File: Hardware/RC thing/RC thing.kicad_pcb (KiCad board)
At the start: 2 copper layers, 56.4 x 52.8 mm, 68 parts, among them J2 2171790001, J2 Conn_01x04, SW1 Bat_switch, SW1 TL3342F160QG_TR, SW2 SW_Push, SW3 SW_Push, SW4 SW_Push, SW5 TL3342F160QG_TR, U1 MCP73831-2-OT, U102 NRF24L01_Breakout, U2 RP2040, U3 W25Q128JVS, U401 TPS62170DSG, Y3 Crystal_GND24_Small

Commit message: RC thing PCB 95% trustworthy (six seven)
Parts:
- removed C30: 100n, Capacitor_SMD:C_0603_1608Metric_Pad1.08x0.95mm_HandSolder
- removed the J2 at (160.2, 68.7)
- removed R25: 100k, Resistor_SMD:R_0603_1608Metric_Pad0.98x0.95mm_HandSolder
- removed R26: 360k, Resistor_SMD:R_0603_1608Metric_Pad0.98x0.95mm_HandSolder
- removed RV3, RV4: 4.7k, Connector_PinHeader_2.54mm:PinHeader_1x03_P2.54mm_Vertical
- removed U102: NRF24L01_Breakout, Connector_PinHeader_2.54mm:PinHeader_2x04_P2.54mm_Vertical
- added C409: 100n, Capacitor_SMD:C_0603_1608Metric_Pad1.08x0.95mm_HandSolder, B.Cu at (126.5, 67.4)
- added J1: Conn_01x04, Connector_PinHeader_2.54mm:PinHeader_1x04_P2.54mm_Vertical, B.Cu at (160.0, 68.5)
- added R410: 100k, Resistor_SMD:R_0603_1608Metric_Pad0.98x0.95mm_HandSolder, B.Cu at (124.5, 67.4)
- added R411: 360k, Resistor_SMD:R_0603_1608Metric_Pad0.98x0.95mm_HandSolder, B.Cu at (128.5, 67.4)
- added RV1: 4.7k, Connector_PinHeader_2.54mm:PinHeader_1x03_P2.54mm_Vertical, B.Cu at (127.5, 75.0)
- added RV2: 4.7k, Connector_PinHeader_2.54mm:PinHeader_1x03_P2.54mm_Vertical, B.Cu at (127.5, 71.0)
- added U101: NRF24L01_Breakout, Connector_PinHeader_2.54mm:PinHeader_2x04_P2.54mm_Vertical, B.Cu at (125.0, 81.0)
- moved SW4 1.85 mm to (156.5, 85.2)
- moved SW2 1.83 mm to (156.5, 76.0)
- moved SW3 1.77 mm to (156.5, 80.5)
- moved R2 0.53 mm to (129.0, 54.5)
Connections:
- D2 pad 1: /BMS and power/Charge_status -> /RP2040/GPIO22
- SW2 pad 2: /RP2040/Button1 -> /Button1
- SW3 pad 2: /RP2040/Button2 -> /Button2
- SW4 pad 2: /RP2040/Button3 -> /Button3
- U1 pad 1: /BMS and power/Charge_status -> /RP2040/GPIO22
- U2 pad 2: /RP2040/GPIO0 -> /SDA
- U2 pad 27: /RP2040/GPIO16 -> /MISO
- U2 pad 29: /RP2040/GPIO18 -> /SCK
- U2 pad 3: /RP2040/GPIO1 -> /SCL
- U2 pad 30: /RP2040/GPIO19 -> /MOSI
- U2 pad 31: /RP2040/GPIO20 -> /CE
- U2 pad 32: /RP2040/GPIO21 -> /CSN
- U2 pad 38: /RP2040/GPIO26_ADC0 -> /AnaStk_1
- U2 pad 39: /RP2040/GPIO27_ADC1 -> /AnaStk_2
- U2 pad 6: /RP2040/GPIO4 -> /Button1
- U2 pad 7: /RP2040/GPIO5 -> /Button2
- U2 pad 8: /RP2040/GPIO6 -> /Button3
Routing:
- net /RP2040/GPIO22: track 0.00 -> 30.2 mm, vias 0 -> 2
- net (no net): track 30.2 -> 0.00 mm
- net /Button3: track 0.00 -> 17.1 mm
- net /RP2040/CSN: track 16.4 -> 0.00 mm
- net /CSN: track 0.00 -> 16.4 mm
- net /RP2040/Battery_voltage_level: track 15.3 -> 0.00 mm
- net /RP2040/GPIO28_ADC2: track 0.00 -> 15.3 mm
- net /RP2040/Button3: track 15.2 -> 0.00 mm
- net /RP2040/MOSI: track 13.4 -> 0.00 mm
- net /MOSI: track 0.00 -> 13.4 mm
- net /Button2: track 0.00 -> 13.2 mm
- net /SCL: track 0.00 -> 13.0 mm
- net /RP2040/SCL: track 13.0 -> 0.00 mm
- net /RP2040/AnaStk_1: track 12.7 -> 0.00 mm
- net /AnaStk_1: track 0.00 -> 12.7 mm
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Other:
- board text added: "SPRO3 RC controller PCB"
- board text added: "sase sapte"
- board text added: "seks syve"
- board text added: "sesi septyni"
- board text added: "sest sedem"

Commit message: new RC PCB updates
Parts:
- removed the R1 at (135.3, 88.5)
- removed the SW1 at (128.8, 89.5)
- added R9: 10k, Capacitor_SMD:C_0603_1608Metric_Pad1.08x0.95mm_HandSolder, F.Cu at (151.3, 96.4)
- added SW8: TL3342F160QG_TR, Main_PCB:SW_TL3342F160QG_TR, F.Cu at (135.2, 50.9)
- ? (x9), H1, H2, H3, H4: moved to B.Cu
- BT1, C1, C10, C11, C12, C13, C14, C15, C16, C18, C2, C20, C3, C4, C5, C6, C8, C9, D1, D2, J1, J2, R1, R10, R2, R3, R4, R5, R6, R7, R8, SW1, SW5, U1, U101, U2, U3, U401, Y3: moved to F.Cu
- C31: renamed from C401; moved to F.Cu
- C32: renamed from C404; moved to F.Cu
- C33: renamed from C409; moved to F.Cu
- L2: renamed from L402; moved to F.Cu
- R35: renamed from R403; moved to F.Cu
- R36: renamed from R405; moved to F.Cu
- R37: renamed from R404; moved to F.Cu
- R38: renamed from R411; moved to F.Cu
- R39: renamed from R410; moved to F.Cu
- RV1, RV2: footprint Connector_PinHeader_2.54mm:PinHeader_1x03_P2.54mm_Vertical -> Connector_JST:JST_PH_B3B-PH-K_1x03_P2.00mm_Vertical; moved to F.Cu
- SW2, SW3, SW4: footprint Connector_PinHeader_2.54mm:PinHeader_1x02_P2.54mm_Vertical -> Connector_JST:JST_PH_B2B-PH-K_1x02_P2.00mm_Vertical; moved to F.Cu
- moved H4 55.3 mm to (171.0, 94.2), turned to 180 degrees
- moved H1 55.2 mm to (170.9, 48.3), turned to 180 degrees
- moved BT1 54.1 mm to (169.4, 59.0)
- moved SW1 54.1 mm to (169.4, 66.5)
- moved SW5 47.9 mm to (144.3, 94.5), turned to 0 degrees
- moved H3 43.5 mm to (120.9, 94.3), turned to 180 degrees
- moved H2 43.4 mm to (120.9, 48.0), turned to 180 degrees
- moved RV1 41.7 mm to (168.6, 81.8), turned to 180 degrees
- moved C31 41.3 mm to (163.3, 67.1), turned to 0 degrees
- moved RV2 41.2 mm to (168.5, 75.0), turned to 180 degrees
- moved C18 39.1 mm to (161.9, 62.0), turned to 0 degrees
- moved R39 36.2 mm to (160.4, 71.5)
- moved J1 35.3 mm to (124.9, 72.5)
- moved U101 35.2 mm to (160.0, 85.0)
- moved U1 34.3 mm to (159.5, 58.4)
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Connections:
- SW5 pad 2: /RP2040/~{USB_BOOT} -> /RP2040/RUN
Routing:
- net +3V3: track 133.8 -> 106.4 mm, vias 8 -> 9
- net VBAT: track 22.9 -> 0.00 mm, vias 0 -> 1
- net /RP2040/RUN: track 0.00 -> 20.6 mm
- net Net-(U2-RUN): track 15.9 -> 0.00 mm
- net /RP2040/XIN: track 16.1 -> 8.28 mm
- net /AnaStk_1: track 12.7 -> 20.3 mm
- net Net-(C3-Pad1): track 6.58 -> 0.00 mm
- net /AnaStk_2: track 12.6 -> 19.0 mm
- net /RP2040/~{USB_BOOT}: track 3.96 -> 10.3 mm
- net +1V1: track 26.4 -> 31.4 mm
- net Net-(U401-SW): track 3.70 -> 0.00 mm
- net /RP2040/XOUT: track 4.16 -> 6.43 mm
- net /Button3: track 17.1 -> 19.0 mm
- net +3.3V: track 0.00 -> 1.66 mm, vias 0 -> 1
- net /Button2: track 13.2 -> 14.4 mm
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- added copper zone on F.Cu, net +1V1
- added copper zone on F.Cu, net +3V3
- added copper zone on In2.Cu, net +3V3
- added copper zone on In1.Cu, net GND
- added copper zone on F.Cu, net Net-(C3-Pad1)
- added copper zone on F.Cu, net Net-(U401-SW)
- added copper zone on F.Cu, net VBAT
- removed copper zone on B.Cu, net +1V1
- removed copper zone on B.Cu, net +3V3
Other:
- board size 56.4 x 52.8 mm -> 58.1 x 54 mm
- copper layers 2 -> 4
- board text removed: "->"
- board text removed: "IN ORDER"
- board text removed: "x2"

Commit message: G will be touched tonight
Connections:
- R9 pad 2: +3.3V -> +3V3
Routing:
- net +3V3: track 106.4 -> 114.1 mm, vias 9 -> 10
- net +3.3V: track 1.66 -> 0.00 mm, vias 1 -> 0
- net VBAT: vias 1 -> 0
- net GND: vias 26 -> 25
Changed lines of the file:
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@@
 	(net 64 "/IRQ")
 	(net 65 "/SCK")
-	(net 66 "+3.3V")
 	(footprint "Resistor_SMD:R_0603_1608Metric_Pad0.98x0.95mm_HandSolder"
 		(layer "F.Cu")
@@
 			(layers "F.Cu" "F.Mask" "F.Paste")
 			(roundrect_rratio 0.25)
-			(net 66 "+3.3V")
+			(net 7 "+3V3")
 			(pintype "passive")
 		)
@@
 		(tags "resistor handsolder")
 		(property "Reference" "R39"
-			(at 0 -1.43 90)
+			(at -0.4625 -1.365375 90)
 			(layer "F.SilkS")
 			(effects
 				(font
-					(size 1 1)
-					(thickness 0.15)
+					(size 0.8 0.8)
+					(thickness 0.1)
 				)
 			)
@@
 		(tags "capacitor handsolder")
 		(property "Reference" "C11"
-			(at 3.1375 0.075 0)
+			(at 0.002875 -1.8 0)
 			(layer "F.SilkS")
 			(effects
@@
 		(net 0)
 	)
-	(via
-		(at 164.759625 69.125)
-		(size 0.45)
-		(drill 0.3)
-		(layers "F.Cu" "B.Cu")
-		(free yes)
-		(net 1)
-	)
 	(segment
 		(start 159.434625 49.540375)
@@
 	)
 	(via
-		(at 162.584625 71.125)
-		(size 0.6)
-		(drill 0.3)
-		(layers "F.Cu" "B.Cu")
-		(net 2)
-	)
-	(via
 		(at 158.984625 61.05)
 		(size 0.6)
@@
 	)
 	(segment
+		(start 153.78 96.38)
+		(end 153.79 96.37)
+		(width 0.4)
+		(layer "F.Cu")
+		(net 7)
+	)
+	(segment
 		(start 147.022125 75.16325)
 		(end 147.022125 74.6375)
@@
 	)
 	(segment
+		(start 168.51 77.8)
+		(end 168.73 78.02)
+		(width 0.4)
+		(layer "F.Cu")
+		(net 7)
+	)
+	(segment
 		(start 148.259625 75.475)
 		(end 147.390375 75.475)
@@
 	)
 	(segment
+		(start 168.62 84.75)
+		(end 168.61 84.76)
+		(width 0.4)
+		(layer "F.Cu")
+		(net 7)
+	)
+	(segment
 		(start 139.584625 75.475)
 		(end 139.334625 75.225)
@@
 	)
 	(segment
+		(start 152.1325 96.38)
+		(end 153.78 96.38)
+		(width 0.4)
+		(layer "F.Cu")
+		(net 7)
+	)
+	(segment
 		(start 141.384625 75.475)
 		(end 139.584625 75.475)
@@
 	)
 	(segment
+		(start 163.24 87.59)
+		(end 163.25 87.6)
+		(width 0.4)
+		(layer "F.Cu")
+		(net 7)
+	)
+	(segment
 		(start 141.384625 79.075)
 		(end 142.309625 79.075)
@@
 	)
 	(segment
+		(start 168.62 81.85)
+		(end 168.62 84.75)
+		(width 0.4)
+		(layer "F.Cu")
+		(net 7)
+	)
+	(segment
 		(start 139.801107 79.075)
 		(end 139.334625 79.541482)
@@
 	)
 	(segment
+		(start 159.974625 87.59)
+		(end 163.24 87.59)
+		(width 0.4)
+		(layer "F.Cu")
+		(net 7)
+	)
+	(segment
+		(start 168.51 74.98)
+		(end 168.51 77.8)
+		(width 0.4)
+		(layer "F.Cu")
+		(net 7)
+	)
+	(segment
 		(start 151.122125 66.676475)
 		(end 151.1236 66.675)
@@
 	)
 	(via
+		(at 153.79 96.37)
+		(size 0.45)
+		(drill 0.3)
+		(layers "F.Cu" "B.Cu")
+		(free yes)
+		(net 7)
+	)
+	(via
 		(at 168.73 78.02)
 		(size 0.45)
@@
 	)
 	(segment
-		(start 163.24 87.59)
-		(end 163.25 87.6)
-		(width 0.4)
-		(layer "In2.Cu")
-		(net 7)
-	)
-	(segment
-		(start 159.974625 87.59)
-		(end 163.24 87.59)
-		(width 0.4)
-		(layer "In2.Cu")
-		(net 7)
-	)
-	(segment
 		(start 158.222125 57.5875)
 		(end 158.534625 57.275)
@@
 		(net 65)
 	)
-	(segment
-		(start 153.78 96.38)
-		(end 153.79 96.37)
-		(width 0.4)
-		(layer "F.Cu")
-		(net 66)
-	)
-	(segment
-		(start 152.1325 96.38)
-		(end 153.78 96.38)
-		(width 0.4)
-		(layer "F.Cu")
-		(net 66)
-	)
-	(via
-		(at 153.79 96.37)
-		(size 0.45)
-		(drill 0.3)
-		(layers "F.Cu" "B.Cu")
-		(net 66)
-	)
 	(zone

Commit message: Reviewed .sch
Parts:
- added R11: 5.1k, Resistor_SMD:R_0603_1608Metric_Pad0.98x0.95mm_HandSolder, F.Cu at (177.9, 59.8)
- added R12: 5.1k, Resistor_SMD:R_0603_1608Metric_Pad0.98x0.95mm_HandSolder, F.Cu at (177.9, 62.3)
- C16: value 10u -> 4.7u
- renumbered Y3 to X1

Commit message: trustworthy(?) RC PCB
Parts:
- J1: footprint Connector_PinHeader_2.54mm:PinHeader_1x04_P2.54mm_Vertical -> Connector_JST:JST_PH_B4B-PH-K_1x04_P2.00mm_Vertical
- moved R12 50.5 mm to (129.1, 75.2)
- moved R11 43.9 mm to (136.5, 74.5), turned to 180 degrees
- moved R36 6.62 mm to (158.6, 65.0), turned to 180 degrees
- moved R37 5.77 mm to (156.8, 63.4)
- moved C32 4.61 mm to (152.3, 65.6), turned to 180 degrees
- moved J1 2.04 mm to (126.2, 71.0), turned to 0 degrees
- moved L2 0.20 mm to (155.5, 66.8)
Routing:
- net /SDA: track 10.3 -> 18.0 mm
- net +3V3: track 114.1 -> 109.2 mm, vias 10 -> 11
- net Net-(U401-FB): track 7.78 -> 3.91 mm
- net /SCL: track 13.0 -> 16.5 mm
- net Net-(U401-SW): track 0.00 -> 2.97 mm
- net GND: track 57.4 -> 57.2 mm, vias 25 -> 31
- net (no net): vias 3 -> 0

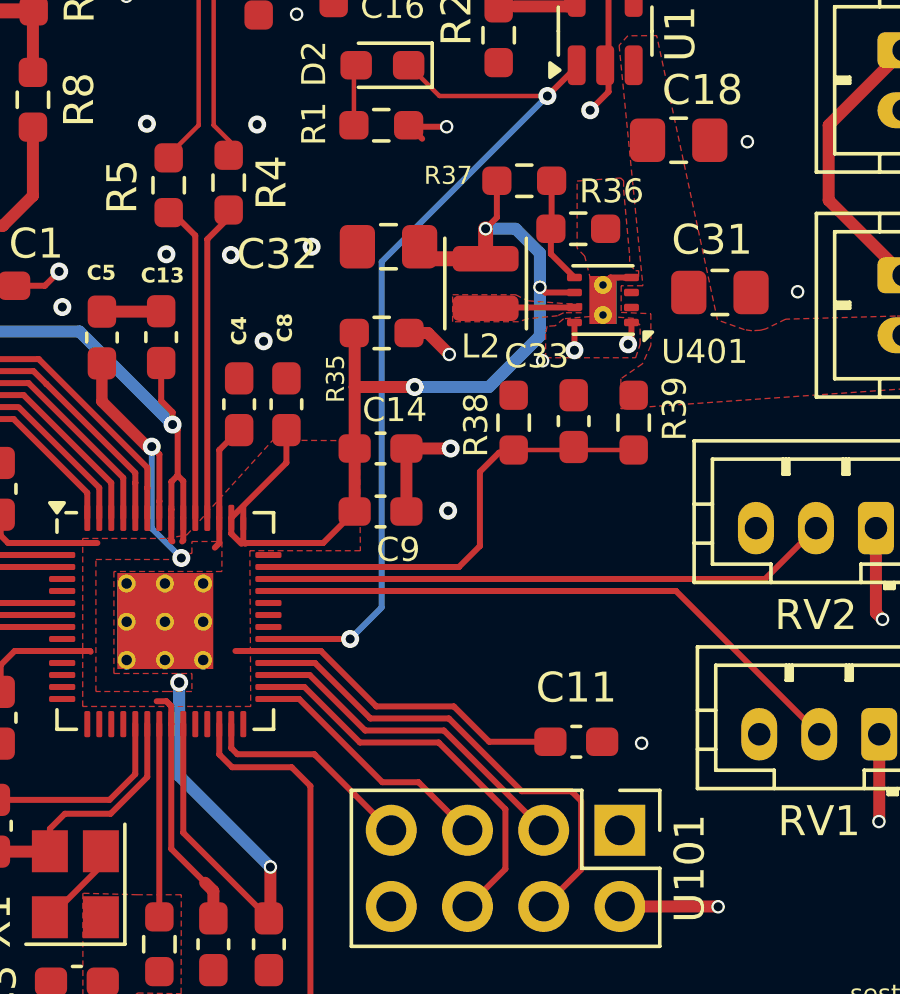
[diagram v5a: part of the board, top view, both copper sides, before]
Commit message: fixing DRC errors on RC
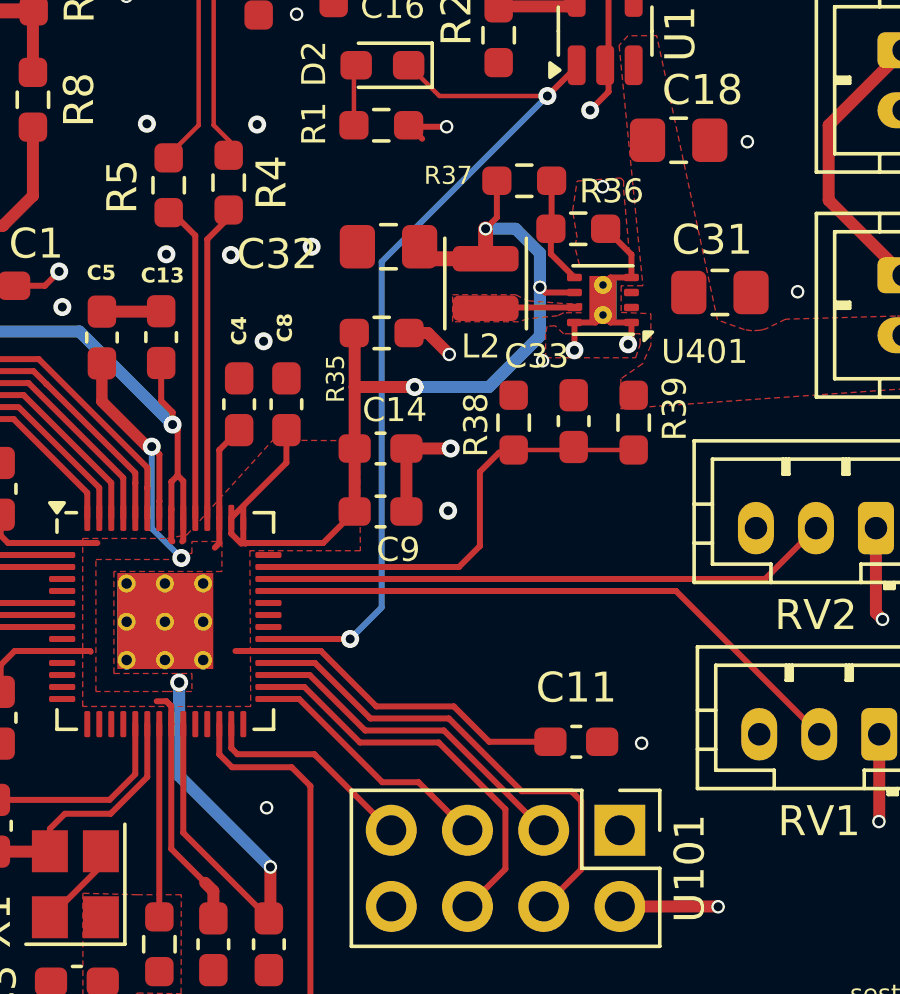
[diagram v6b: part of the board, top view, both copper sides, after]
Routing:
- net GND: track 57.2 -> 61.3 mm, vias 31 -> 33
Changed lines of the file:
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@@
 	)
 	(segment
+		(start 158.4611 68.125)
+		(end 159.1611 68.125)
+		(width 0.2)
+		(layer "F.Cu")
+		(net 2)
+	)
+	(segment
 		(start 143.434625 57.159625)
 		(end 143.525 57.25)
@@
 	)
 	(segment
+		(start 159.1611 68.125)
+		(end 159.4111 67.875)
+		(width 0.2)
+		(layer "F.Cu")
+		(net 2)
+	)
+	(segment
 		(start 137.802125 82.1625)
 		(end 137.774625 82.19)
@@
 	)
 	(segment
+		(start 159.6611 68.125)
+		(end 159.4111 67.875)
+		(width 0.2)
+		(layer "F.Cu")
+		(net 2)
+	)
+	(segment
 		(start 144.822125 78.075)
 		(end 144.822125 78.1125)
@@
 	)
 	(segment
+		(start 160.3611 65.8611)
+		(end 159.5 65)
+		(width 0.2)
+		(layer "F.Cu")
+		(net 2)
+	)
+	(segment
 		(start 159.6611 66.625)
 		(end 159.4111 66.875)
@@
 	)
 	(segment
+		(start 160.3611 68.125)
+		(end 159.6611 68.125)
+		(width 0.2)
+		(layer "F.Cu")
+		(net 2)
+	)
+	(segment
 		(start 143.822125 81.5125)
 		(end 143.822125 83.181487)
@@
 	)
 	(segment
+		(start 160.3611 66.625)
+		(end 160.3611 65.8611)
+		(width 0.2)
+		(layer "F.Cu")
+		(net 2)
+	)
+	(segment
 		(start 159.597125 55.847125)
 		(end 159.597125 60.4375)
@@
 	)
 	(via
+		(at 148.2 84.3)
+		(size 0.45)
+		(drill 0.3)
+		(layers "F.Cu" "B.Cu")
+		(free yes)
+		(net 2)
+	)
+	(via
 		(at 164.225 62.1)
 		(size 0.45)
@@
 	)
 	(via
+		(at 159.4 63.6)
+		(size 0.45)
+		(drill 0.3)
+		(layers "F.Cu" "B.Cu")
+		(free yes)
+		(net 2)
+	)
+	(via
 		(at 147.884625 61.525)
 		(size 0.6)
@@
 			(thermal_gap 0.508)
 			(thermal_bridge_width 0.508)
-			(island_removal_mode 1)
-			(island_area_min 10)
 		)
 		(polygon
@@
 		(polygon
 			(pts
-				(xy 160.5 69.3) (xy 160.65 68.85) (xy 160.65 68.215384) (xy 160.439085 67.987622) (xy 159.3 67.9)
-				(xy 158.1 68) (xy 157.819672 68.233607) (xy 157.55 68.25) (xy 157.5 68.499999) (xy 157.5 69.3)
+				(xy 160.5 69.3) (xy 160.65 68.85) (xy 160.65 68.5) (xy 160 68.5) (xy 159.3 68.5) (xy 158.1 68.5)
+				(xy 157.819672 68.233607) (xy 157.55 68.25) (xy 157.5 68.499999) (xy 157.5 69.3)
 			)
 		)
@@
 		(polygon
 			(pts
-				(xy 160.6 66.7) (xy 159 66.7) (xy 158.802941 65.911765) (xy 158.55 65.65) (xy 158.55 65.3) (xy 158.55 63.410714)
-				(xy 160.000254 63.307125) (xy 160.1 63.4) (xy 160.1 63.7) (xy 160.3 65.9) (xy 160.3 66.2) (xy 160.5 66.4)
-				(xy 160.6 66.4)
+				(xy 158.625 66.2) (xy 158.465686 65.562745) (xy 158.55 65.300007) (xy 158.4 64.4) (xy 158.55 63.410714)
+				(xy 160.000254 63.307125) (xy 160.1 63.4) (xy 160.1 63.7) (xy 160.3 65.9) (xy 160.3 66.2)
 			)
 		)

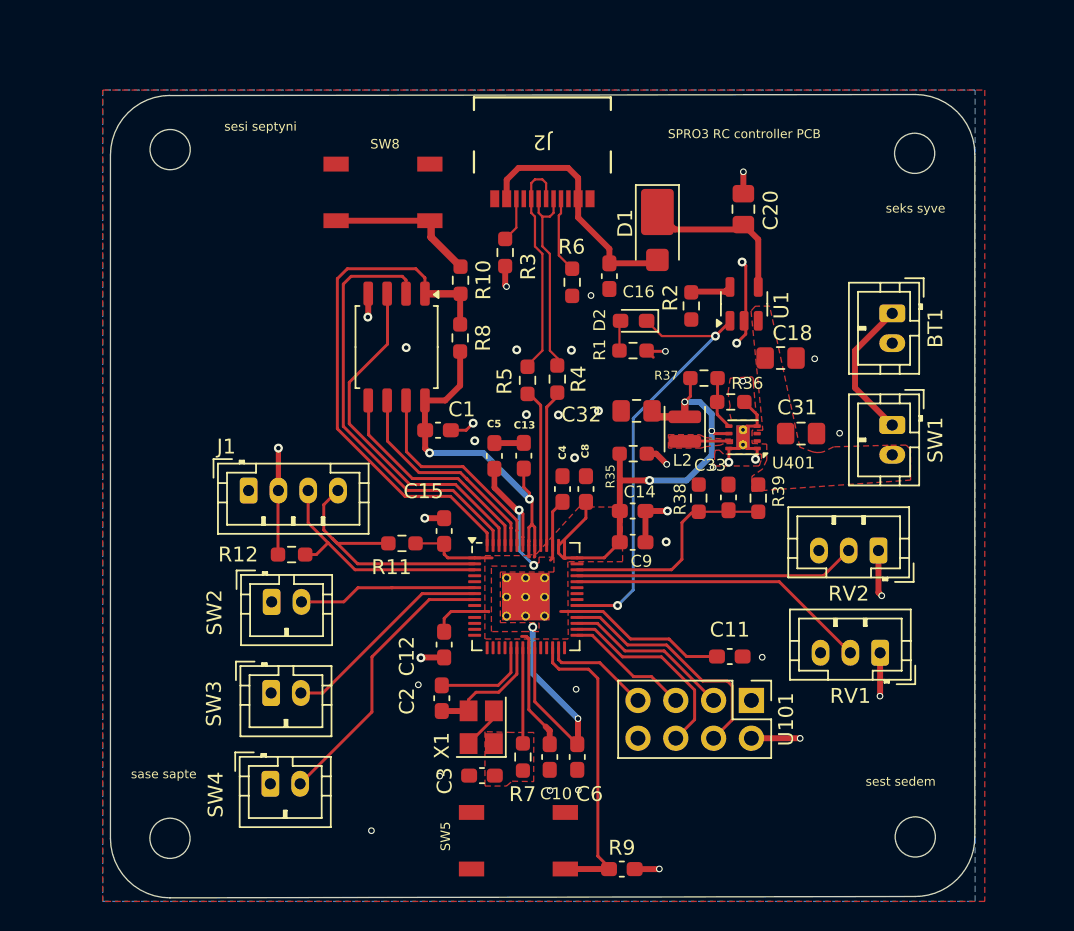
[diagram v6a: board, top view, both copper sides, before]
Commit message: Stitching GND, silkscreen thickness, increased thermal distribution of charger IC
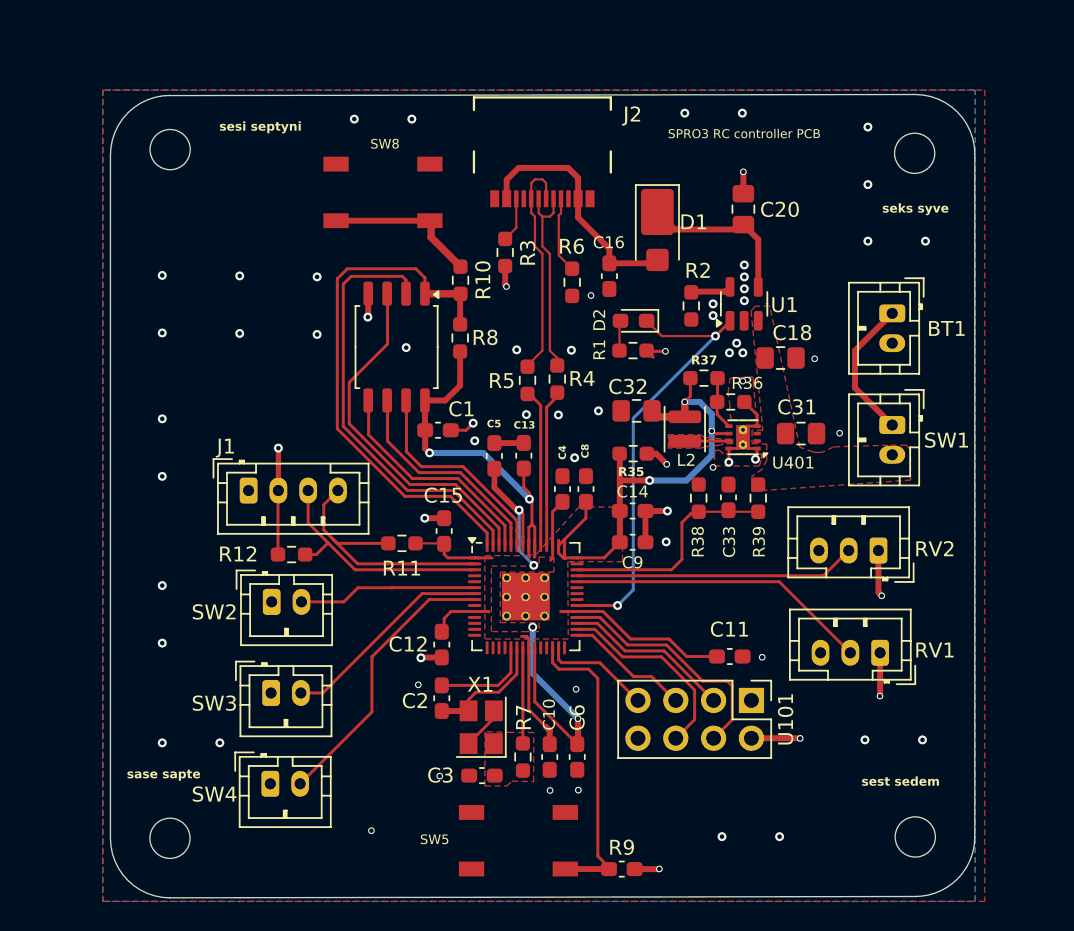
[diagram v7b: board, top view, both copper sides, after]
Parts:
- moved C12 0.16 mm to (139.2, 81.3)
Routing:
- net GND: track 61.3 -> 55.5 mm, vias 33 -> 64
